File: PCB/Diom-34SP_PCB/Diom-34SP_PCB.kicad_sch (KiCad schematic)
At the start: 19 parts, among them J1 Conn_01x02_Male, U1 nice_nano

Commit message: Mounting Holes added
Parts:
- added H1: (no value), symbol Mechanical:MountingHole
- added H10, H2, H3, H4, H5, H6, H7, H8, H9: MountingHole, MountingHole:MountingHole_2.2mm_M2_DIN965, symbol Mechanical:MountingHole
- MX17: value (none) -> MX-NoLED; footprint (none) -> mx-switches-doubleSided:CherryMX-1.5U-doubleSided-Vertical
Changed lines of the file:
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@@
       (effects (font (size 1.524 1.524)))
     )
-    (property "Value" "" (id 1) (at 199.0056 91.44 0)
-      (effects (font (size 0.508 0.508)))
-    )
-    (property "Footprint" "" (id 2) (at 182.245 97.155 0)
+    (property "Value" "MX-NoLED" (id 1) (at 199.0056 91.44 0)
+      (effects (font (size 0.508 0.508)))
+    )
+    (property "Footprint" "mx-switches-doubleSided:CherryMX-1.5U-doubleSided-Vertical" (id 2) (at 182.245 97.155 0)
       (effects (font (size 1.524 1.524)) hide)
     )
@@
     (pin "1")
     (pin "2")
+  )
+  (symbol (lib_id "Mechanical:MountingHole") (at 201.93 34.29 0) (unit 1)
+    (in_bom yes) (on_board yes)
+    (property "Reference" "H7" (id 0) (at 204.47 33.0199 0)
+      (effects (font (size 1.27 1.27)) (justify left))
+    )
+    (property "Value" "MountingHole" (id 1) (at 204.47 35.5599 0)
+      (effects (font (size 1.27 1.27)) (justify left))
+    )
+    (property "Footprint" "MountingHole:MountingHole_2.2mm_M2_DIN965" (id 2) (at 201.93 34.29 0)
+      (effects (font (size 1.27 1.27)) hide)
+    )
+    (property "Datasheet" "~" (id 3) (at 201.93 34.29 0)
+      (effects (font (size 1.27 1.27)) hide)
+    )
   )
   (symbol (lib_id "power:GND") (at 185.42 100.33 0) (unit 1)
@@
     (pin "2")
   )
+  (symbol (lib_id "Mechanical:MountingHole") (at 222.25 57.15 0) (unit 1)
+    (in_bom yes) (on_board yes)
+    (property "Reference" "H10" (id 0) (at 224.79 55.8799 0)
+      (effects (font (size 1.27 1.27)) (justify left))
+    )
+    (property "Value" "MountingHole" (id 1) (at 224.79 58.4199 0)
+      (effects (font (size 1.27 1.27)) (justify left))
+    )
+    (property "Footprint" "MountingHole:MountingHole_2.2mm_M2_DIN965" (id 2) (at 222.25 57.15 0)
+      (effects (font (size 1.27 1.27)) hide)
+    )
+    (property "Datasheet" "~" (id 3) (at 222.25 57.15 0)
+      (effects (font (size 1.27 1.27)) hide)
+    )
+  )
   (symbol (lib_id "power:GND") (at 185.42 80.01 0) (unit 1)
     (in_bom yes) (on_board yes) (fields_autoplaced)
@@
     (pin "1")
   )
+  (symbol (lib_id "Mechanical:MountingHole") (at 201.93 57.15 0) (unit 1)
+    (in_bom yes) (on_board yes)
+    (property "Reference" "H8" (id 0) (at 204.47 55.8799 0)
+      (effects (font (size 1.27 1.27)) (justify left))
+    )
+    (property "Value" "MountingHole" (id 1) (at 204.47 58.4199 0)
+      (effects (font (size 1.27 1.27)) (justify left))
+    )
+    (property "Footprint" "MountingHole:MountingHole_2.2mm_M2_DIN965" (id 2) (at 201.93 57.15 0)
+      (effects (font (size 1.27 1.27)) hide)
+    )
+    (property "Datasheet" "~" (id 3) (at 201.93 57.15 0)
+      (effects (font (size 1.27 1.27)) hide)
+    )
+  )
+  (symbol (lib_id "Mechanical:MountingHole") (at 213.36 88.9 0) (unit 1)
+    (in_bom yes) (on_board yes) (fields_autoplaced)
+    (property "Reference" "H3" (id 0) (at 215.9 87.6299 0)
+      (effects (font (size 1.27 1.27)) (justify left))
+    )
+    (property "Value" "MountingHole" (id 1) (at 215.9 90.1699 0)
+      (effects (font (size 1.27 1.27)) (justify left))
+    )
+    (property "Footprint" "MountingHole:MountingHole_2.2mm_M2_DIN965" (id 2) (at 213.36 88.9 0)
+      (effects (font (size 1.27 1.27)) hide)
+    )
+    (property "Datasheet" "~" (id 3) (at 213.36 88.9 0)
+      (effects (font (size 1.27 1.27)) hide)
+    )
+  )
   (symbol (lib_id "power:GND") (at 139.7 44.45 0) (unit 1)
     (in_bom yes) (on_board yes) (fields_autoplaced)
@@
     (pin "1")
   )
+  (symbol (lib_id "Mechanical:MountingHole") (at 123.19 35.56 0) (unit 1)
+    (in_bom yes) (on_board yes)
+    (property "Reference" "H1" (id 0) (at 125.73 34.2899 0)
+      (effects (font (size 1.27 1.27)) (justify left))
+    )
+    (property "Value" "" (id 1) (at 125.73 36.8299 0)
+      (effects (font (size 1.27 1.27)) (justify left))
+    )
+    (property "Footprint" "" (id 2) (at 123.19 35.56 0)
+      (effects (font (size 1.27 1.27)) hide)
+    )
+    (property "Datasheet" "~" (id 3) (at 123.19 35.56 0)
+      (effects (font (size 1.27 1.27)) hide)
+    )
+  )
   (symbol (lib_id "power:GND") (at 173.99 80.01 0) (unit 1)
     (in_bom yes) (on_board yes) (fields_autoplaced)
@@
     )
     (pin "1")
+  )
+  (symbol (lib_id "Mechanical:MountingHole") (at 121.92 86.36 0) (unit 1)
+    (in_bom yes) (on_board yes) (fields_autoplaced)
+    (property "Reference" "H2" (id 0) (at 124.46 85.0899 0)
+      (effects (font (size 1.27 1.27)) (justify left))
+    )
+    (property "Value" "MountingHole" (id 1) (at 124.46 87.6299 0)
+      (effects (font (size 1.27 1.27)) (justify left))
+    )
+    (property "Footprint" "MountingHole:MountingHole_2.2mm_M2_DIN965" (id 2) (at 121.92 86.36 0)
+      (effects (font (size 1.27 1.27)) hide)
+    )
+    (property "Datasheet" "~" (id 3) (at 121.92 86.36 0)
+      (effects (font (size 1.27 1.27)) hide)
+    )
   )
   (symbol (lib_id "power:GND") (at 162.56 62.23 0) (unit 1)
@@
     (pin "1")
     (pin "2")
+  )
+  (symbol (lib_id "Mechanical:MountingHole") (at 222.25 34.29 0) (unit 1)
+    (in_bom yes) (on_board yes)
+    (property "Reference" "H9" (id 0) (at 224.79 33.0199 0)
+      (effects (font (size 1.27 1.27)) (justify left))
+    )
+    (property "Value" "MountingHole" (id 1) (at 224.79 35.5599 0)
+      (effects (font (size 1.27 1.27)) (justify left))
+    )
+    (property "Footprint" "MountingHole:MountingHole_2.2mm_M2_DIN965" (id 2) (at 222.25 34.29 0)
+      (effects (font (size 1.27 1.27)) hide)
+    )
+    (property "Datasheet" "~" (id 3) (at 222.25 34.29 0)
+      (effects (font (size 1.27 1.27)) hide)
+    )
+  )
+  (symbol (lib_id "Mechanical:MountingHole") (at 160.02 88.9 0) (unit 1)
+    (in_bom yes) (on_board yes) (fields_autoplaced)
+    (property "Reference" "H6" (id 0) (at 162.56 87.6299 0)
+      (effects (font (size 1.27 1.27)) (justify left))
+    )
+    (property "Value" "MountingHole" (id 1) (at 162.56 90.1699 0)
+      (effects (font (size 1.27 1.27)) (justify left))
+    )
+    (property "Footprint" "MountingHole:MountingHole_2.2mm_M2_DIN965" (id 2) (at 160.02 88.9 0)
+      (effects (font (size 1.27 1.27)) hide)
+    )
+    (property "Datasheet" "~" (id 3) (at 160.02 88.9 0)
+      (effects (font (size 1.27 1.27)) hide)
+    )
+  )
+  (symbol (lib_id "Mechanical:MountingHole") (at 212.09 105.41 0) (unit 1)
+    (in_bom yes) (on_board yes)
+    (property "Reference" "H4" (id 0) (at 214.63 104.14 0)
+      (effects (font (size 1.27 1.27)) (justify left))
+    )
+    (property "Value" "MountingHole" (id 1) (at 214.63 106.6799 0)
+      (effects (font (size 1.27 1.27)) (justify left))
+    )
+    (property "Footprint" "MountingHole:MountingHole_2.2mm_M2_DIN965" (id 2) (at 212.09 105.41 0)
+      (effects (font (size 1.27 1.27)) hide)
+    )
+    (property "Datasheet" "~" (id 3) (at 212.09 105.41 0)
+      (effects (font (size 1.27 1.27)) hide)
+    )
   )
   (symbol (lib_id "MX_Alps_Hybrid:MX-NoLED") (at 163.83 58.42 0) (unit 1)
@@
     (pin "1")
   )
+  (symbol (lib_id "Mechanical:MountingHole") (at 171.45 29.21 0) (unit 1)
+    (in_bom yes) (on_board yes)
+    (property "Reference" "H5" (id 0) (at 173.99 27.9399 0)
+      (effects (font (size 1.27 1.27)) (justify left))
+    )
+    (property "Value" "MountingHole" (id 1) (at 173.99 30.4799 0)
+      (effects (font (size 1.27 1.27)) (justify left))
+    )
+    (property "Footprint" "MountingHole:MountingHole_2.2mm_M2_DIN965" (id 2) (at 171.45 29.21 0)
+      (effects (font (size 1.27 1.27)) hide)
+    )
+    (property "Datasheet" "~" (id 3) (at 171.45 29.21 0)
+      (effects (font (size 1.27 1.27)) hide)
+    )
+  )
   (symbol (lib_id "MX_Alps_Hybrid:MX-NoLED") (at 140.97 40.64 0) (unit 1)
     (in_bom yes) (on_board yes) (fields_autoplaced)
@@
       (reference "#PWR022") (unit 1) (value "GND") (footprint "")
     )
+    (path "/78ede9a5-24b2-446b-883e-d0eb187e6d79"
+      (reference "H1") (unit 1) (value "MountingHole") (footprint "MountingHole:MountingHole_2.2mm_M2_DIN965")
+    )
+    (path "/91eb9ba5-74ad-4ad5-b139-23d963b97aa2"
+      (reference "H2") (unit 1) (value "MountingHole") (footprint "MountingHole:MountingHole_2.2mm_M2_DIN965")
+    )
+    (path "/63bc4bcd-f5ab-4033-ab29-d1e3934aa3c9"
+      (reference "H3") (unit 1) (value "MountingHole") (footprint "MountingHole:MountingHole_2.2mm_M2_DIN965")
+    )
+    (path "/b029e962-2343-4662-b431-ffc97673b67a"
+      (reference "H4") (unit 1) (value "MountingHole") (footprint "MountingHole:MountingHole_2.2mm_M2_DIN965")
+    )
+    (path "/fb256c68-3c79-4a8e-a56c-e9920d041772"
+      (reference "H5") (unit 1) (value "MountingHole") (footprint "MountingHole:MountingHole_2.2mm_M2_DIN965")
+    )
+    (path "/ad38594d-2662-4d9f-8203-2caaa7d508bf"
+      (reference "H6") (unit 1) (value "MountingHole") (footprint "MountingHole:MountingHole_2.2mm_M2_DIN965")
+    )
+    (path "/2f26bb7e-fc79-4c7a-9f3a-5c9302f43f53"
+      (reference "H7") (unit 1) (value "MountingHole") (footprint "MountingHole:MountingHole_2.2mm_M2_DIN965")
+    )
+    (path "/5ecfe145-84a4-40b1-8e64-52aab4b20118"
+      (reference "H8") (unit 1) (value "MountingHole") (footprint "MountingHole:MountingHole_2.2mm_M2_DIN965")
+    )
+    (path "/aadf1378-f113-4018-82c7-2eb07f25151b"
+      (reference "H9") (unit 1) (value "MountingHole") (footprint "MountingHole:MountingHole_2.2mm_M2_DIN965")
+    )
+    (path "/498f781b-3751-4805-b650-e622284f42dc"
+      (reference "H10") (unit 1) (value "MountingHole") (footprint "MountingHole:MountingHole_2.2mm_M2_DIN965")
+    )
     (path "/94e4172f-7d42-4a20-80ff-c56fc225b287"

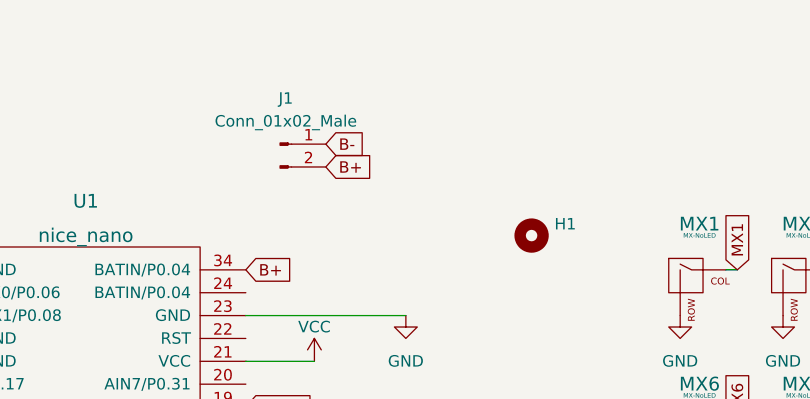
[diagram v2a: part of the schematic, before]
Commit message: Added On/Off Switch
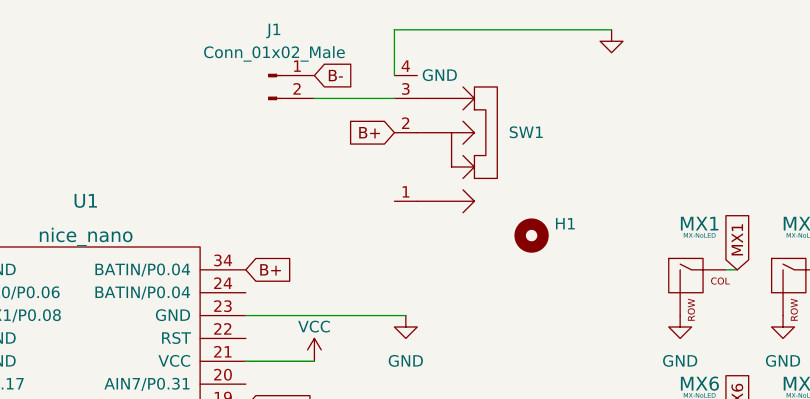
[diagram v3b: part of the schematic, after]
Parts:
- added SW1: (no value), symbol randomSymbols:SHOU_HAN_MSK12C02-HB
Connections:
- net B+: now also SW1.2; no longer J1.2 (Pin_2)
- net GND: now also SW1.4 (GND)
- new net: J1.2 (Pin_2), SW1.3
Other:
- moved on the sheet: J1
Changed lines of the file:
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@@
+    (stroke (width 0) (type default) (color 0 0 0 0))
+  )
+  (wire (pts (xy 132.08 12.7) (xy 107.95 12.7))
     (stroke (width 0) (type default) (color 0 0 0 0))
   )
@@
     (stroke (width 0) (type default) (color 0 0 0 0))
   )
+  (wire (pts (xy 107.95 12.7) (xy 107.95 17.78))
+    (stroke (width 0) (type default) (color 0 0 0 0))
+  )
   (wire (pts (xy 168.91 39.37) (xy 167.64 39.37))
     (stroke (width 0) (type default) (color 0 0 0 0))
   )
   (wire (pts (xy 157.48 57.15) (xy 156.21 57.15))
+    (stroke (width 0) (type default) (color 0 0 0 0))
+  )
+  (wire (pts (xy 99.06 20.32) (xy 107.95 20.32))
     (stroke (width 0) (type default) (color 0 0 0 0))
   )
@@
     )
   )
-  (global_label "B-" (shape input) (at 100.33 25.4 0) (fields_autoplaced)
-    (effects (font (size 1.27 1.27)) (justify left))
-    (property "Intersheet References" "${INTERSHEET_REFS}" (id 0) (at 105.5855 25.4794 0)
+  (global_label "B-" (shape input) (at 99.06 17.78 0) (fields_autoplaced)
+    (effects (font (size 1.27 1.27)) (justify left))
+    (property "Intersheet References" "${INTERSHEET_REFS}" (id 0) (at 104.3155 17.8594 0)
       (effects (font (size 1.27 1.27)) (justify left) hide)
     )
@@
     )
   )
-  (global_label "B+" (shape input) (at 100.33 27.94 0) (fields_autoplaced)
-    (effects (font (size 1.27 1.27)) (justify left))
-    (property "Intersheet References" "${INTERSHEET_REFS}" (id 0) (at 105.5855 27.8606 0)
-      (effects (font (size 1.27 1.27)) (justify left) hide)
+  (global_label "B+" (shape input) (at 107.95 24.13 180) (fields_autoplaced)
+    (effects (font (size 1.27 1.27)) (justify right))
+    (property "Intersheet References" "${INTERSHEET_REFS}" (id 0) (at 102.6945 24.2094 0)
+      (effects (font (size 1.27 1.27)) (justify right) hide)
     )
   )
@@
     (pin "1")
   )
+  (symbol (lib_id "randomSymbols:SHOU_HAN_MSK12C02-HB") (at 119.38 24.13 90) (unit 1)
+    (in_bom yes) (on_board yes) (fields_autoplaced)
+    (property "Reference" "SW1" (id 0) (at 120.65 24.1299 90)
+      (effects (font (size 1.27 1.27)) (justify right))
+    )
+    (property "Value" "" (id 1) (at 120.65 26.6699 90)
+      (effects (font (size 1.27 1.27)) (justify right))
+    )
+    (property "Footprint" "" (id 2) (at 119.38 24.13 0)
+      (effects (font (size 1.27 1.27)) hide)
+    )
+    (property "Datasheet" "" (id 3) (at 119.38 24.13 0)
+      (effects (font (size 1.27 1.27)) hide)
+    )
+    (pin "1")
+    (pin "2")
+    (pin "3")
+    (pin "4")
+  )
   (symbol (lib_id "power:GND") (at 173.99 44.45 0) (unit 1)
     (in_bom yes) (on_board yes) (fields_autoplaced)
@@
     (pin "2")
   )
-  (symbol (lib_id "Connector:Conn_01x02_Male") (at 95.25 25.4 0) (unit 1)
-    (in_bom yes) (on_board yes) (fields_autoplaced)
-    (property "Reference" "J1" (id 0) (at 95.885 20.32 0))
-    (property "Value" "Conn_01x02_Male" (id 1) (at 95.885 22.86 0))
-    (property "Footprint" "Connector_JST:JST_EH_S2B-EH_1x02_P2.50mm_Horizontal" (id 2) (at 95.25 25.4 0)
-      (effects (font (size 1.27 1.27)) hide)
-    )
-    (property "Datasheet" "~" (id 3) (at 95.25 25.4 0)
+  (symbol (lib_id "Connector:Conn_01x02_Male") (at 93.98 17.78 0) (unit 1)
+    (in_bom yes) (on_board yes) (fields_autoplaced)
+    (property "Reference" "J1" (id 0) (at 94.615 12.7 0))
+    (property "Value" "Conn_01x02_Male" (id 1) (at 94.615 15.24 0))
+    (property "Footprint" "Connector_JST:JST_EH_S2B-EH_1x02_P2.50mm_Horizontal" (id 2) (at 93.98 17.78 0)
+      (effects (font (size 1.27 1.27)) hide)
+    )
+    (property "Datasheet" "~" (id 3) (at 93.98 17.78 0)
       (effects (font (size 1.27 1.27)) hide)
     )
@@
       (effects (font (size 1.27 1.27)) hide)
     )
+  )
+  (symbol (lib_id "power:GND") (at 132.08 12.7 0) (unit 1)
+    (in_bom yes) (on_board yes) (fields_autoplaced)
+    (property "Reference" "#PWR0101" (id 0) (at 132.08 19.05 0)
+      (effects (font (size 1.27 1.27)) hide)
+    )
+    (property "Value" "" (id 1) (at 132.08 17.78 0))
+    (property "Footprint" "" (id 2) (at 132.08 12.7 0)
+      (effects (font (size 1.27 1.27)) hide)
+    )
+    (property "Datasheet" "" (id 3) (at 132.08 12.7 0)
+      (effects (font (size 1.27 1.27)) hide)
+    )
+    (pin "1")
   )
   (symbol (lib_id "MX_Alps_Hybrid:MX-NoLED") (at 163.83 58.42 0) (unit 1)
@@
       (reference "#PWR022") (unit 1) (value "GND") (footprint "")
     )
+    (path "/c229ad58-3c1b-4995-a555-52c7a8b54608"
+      (reference "#PWR0101") (unit 1) (value "GND") (footprint "")
+    )
     (path "/78ede9a5-24b2-446b-883e-d0eb187e6d79"
       (reference "H1") (unit 1) (value "MountingHole") (footprint "MountingHole:MountingHole_2.2mm_M2_DIN965")
@@
       (reference "MX17") (unit 1) (value "MX-NoLED") (footprint "mx-switches-doubleSided:CherryMX-1.5U-doubleSided-Vertical")
     )
+    (path "/3849c2dd-7ee7-4eec-9b9d-cb0b329cdea0"
+      (reference "SW1") (unit 1) (value "SHOU_HAN_MSK12C02-HB") (footprint "led:SHOU HAN MSK12C02-HB")
+    )
     (path "/c99fab98-5932-4f1b-aaaf-cb9175d41480"
